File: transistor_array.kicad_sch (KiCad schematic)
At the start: 4 parts, among them Q13 MMBT3904_C181119, Q30 MMBT3904_C181119, Q31 MMBT3904_C181119, Q32 MMBT3904_C181119

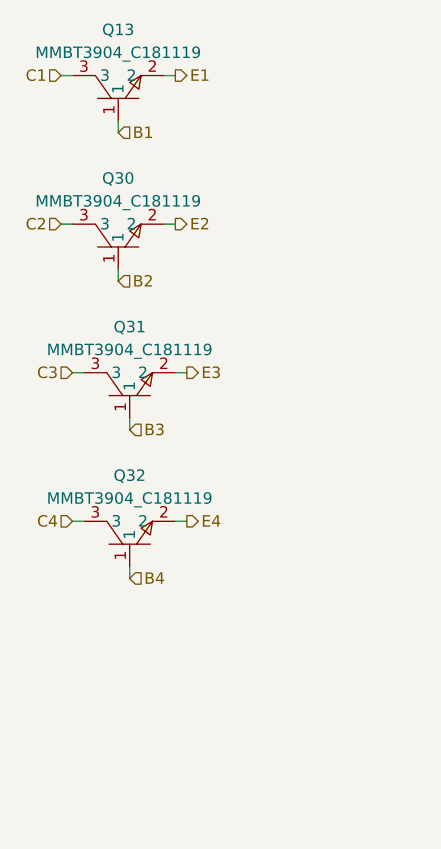
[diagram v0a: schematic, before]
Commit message: Issue #1: Revised possible PCB design
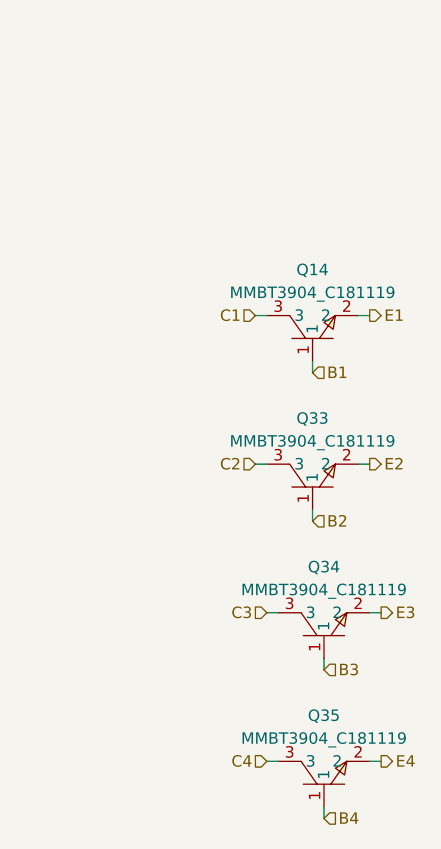
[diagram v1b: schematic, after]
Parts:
- renumbered Q13 to Q14, Q30 to Q33, Q31 to Q34, Q32 to Q35
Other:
- moved on the sheet: Q14, Q33, Q34, Q35

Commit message: Issue #1: Prepare for production
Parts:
- renumbered Q14 to Q2, Q33 to Q3, Q34 to Q4, Q35 to Q5
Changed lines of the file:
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@@
 		(dnp no)
 		(fields_autoplaced yes)
-		(property "Reference" "Q14"
+		(property "Reference" "Q2"
 			(at 72.39 69.85 90)
 			(effects
@@
 		(property "Sim.Type" ""
 			(at 72.39 77.47 0)
+			(effects
+				(font
+					(size 1.27 1.27)
+				)
+				(hide yes)
+			)
+		)
+		(property "LCSP Part" ""
+			(at 72.39 77.47 90)
 			(effects
 				(font
@@
 			(project "rover-chasis-controller"
 				(path "/d124dc5a-4ec5-4298-b967-2d3e405008a3/85e9028e-a593-4694-a303-1fd0a5ed20c6"
-					(reference "Q14")
+					(reference "Q2")
 					(unit 1)
 				)
@@
 		(dnp no)
 		(fields_autoplaced yes)
-		(property "Reference" "Q33"
+		(property "Reference" "Q3"
 			(at 72.39 86.36 90)
 			(effects
@@
 		(property "Sim.Type" ""
 			(at 72.39 93.98 0)
+			(effects
+				(font
+					(size 1.27 1.27)
+				)
+				(hide yes)
+			)
+		)
+		(property "LCSP Part" ""
+			(at 72.39 93.98 90)
 			(effects
 				(font
@@
 			(project "rover-chasis-controller"
 				(path "/d124dc5a-4ec5-4298-b967-2d3e405008a3/85e9028e-a593-4694-a303-1fd0a5ed20c6"
-					(reference "Q33")
+					(reference "Q3")
 					(unit 1)
 				)
@@
 		(dnp no)
 		(fields_autoplaced yes)
-		(property "Reference" "Q35"
+		(property "Reference" "Q5"
 			(at 73.66 119.38 90)
 			(effects
@@
 		(property "Sim.Type" ""
 			(at 73.66 127 0)
+			(effects
+				(font
+					(size 1.27 1.27)
+				)
+				(hide yes)
+			)
+		)
+		(property "LCSP Part" ""
+			(at 73.66 127 90)
 			(effects
 				(font
@@
 			(project "rover-chasis-controller"
 				(path "/d124dc5a-4ec5-4298-b967-2d3e405008a3/85e9028e-a593-4694-a303-1fd0a5ed20c6"
-					(reference "Q35")
+					(reference "Q5")
 					(unit 1)
 				)
@@
 		(dnp no)
 		(fields_autoplaced yes)
-		(property "Reference" "Q34"
+		(property "Reference" "Q4"
 			(at 73.66 102.87 90)
 			(effects
@@
 		(property "Sim.Type" ""
 			(at 73.66 110.49 0)
+			(effects
+				(font
+					(size 1.27 1.27)
+				)
+				(hide yes)
+			)
+		)
+		(property "LCSP Part" ""
+			(at 73.66 110.49 90)
 			(effects
 				(font
@@
 			(project "rover-chasis-controller"
 				(path "/d124dc5a-4ec5-4298-b967-2d3e405008a3/85e9028e-a593-4694-a303-1fd0a5ed20c6"
-					(reference "Q34")
+					(reference "Q4")
 					(unit 1)
 				)
